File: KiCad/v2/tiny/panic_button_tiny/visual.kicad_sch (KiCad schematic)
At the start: 1 part, among them U4 TPS61022

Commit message: [UPDATE] some connections in the schematic
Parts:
- removed U4: TPS61022, Package_DFN_QFN:Texas_RWU0007A_VQFN-7_2x2mm_P0.5mm, symbol Converter_DCDC:TPS61022
- added D1: WS2812B, PCM_SparkFun-LED:WS2812_2020, symbol PCM_SparkFun-LED:WS2812B_2020
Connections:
- net 3.3V: now also D1.4 (VDD)
- net GND: now also D1.2 (VSS)
- new net LED_DIN: D1.3 (DIN)
- no-connect marks 0 -> 1
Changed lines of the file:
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@@
 	(generator_version "10.0")
 	(paper "A4")
-	(wire
-		(pts
-			(xy 62.23 30.48) (xy 60.96 30.48)
-		)
-		(stroke
-			(width 0)
-			(type default)
-		)
-	)
-	(hierarchical_label "modem_status"
+	(no_connect
+		(at 52.07 31.75)
+	)
+	(hierarchical_label "LED_DIN"
 		(shape input)
-		(at 55.88 22.86 90)
+		(at 36.83 31.75 180)
 		(effects
 			(font
 				(size 1.27 1.27)
 			)
-			(justify left)
-		)
-	)
-	(hierarchical_label "modem_rail_switch"
-		(shape input)
-		(at 40.64 30.48 180)
-		(effects
-			(font
-				(size 1.27 1.27)
-			)
 			(justify right)
 		)
@@
 	(symbol
 		(lib_id "PCM_SparkFun-PowerSymbol:3.3V")
-		(at 45.72 22.86 0)
+		(at 44.45 24.13 0)
 		(unit 1)
 		(body_style 1)
@@
 		(dnp no)
 		(fields_autoplaced yes)
-		(property "Reference" "#PWR048"
-			(at 45.72 26.67 0)
+		(property "Reference" "#PWR064"
+			(at 44.45 27.94 0)
 			(hide yes)
 			(show_name no)
@@
 		)
 		(property "Value" "3.3V"
-			(at 45.72 19.05 0)
+			(at 44.45 20.32 0)
 			(show_name no)
 			(do_not_autoplace yes)
@@
 		)
 		(property "Footprint" ""
-			(at 45.72 22.86 0)
+			(at 44.45 24.13 0)
 			(hide yes)
 			(show_name no)
@@
 		)
 		(property "Datasheet" ""
-			(at 45.72 22.86 0)
+			(at 44.45 24.13 0)
 			(hide yes)
 			(show_name no)
@@
 		)
 		(property "Description" "Power symbol creates a global label with name \"3.3V\""
-			(at 45.72 29.21 0)
+			(at 44.45 30.48 0)
 			(hide yes)
 			(show_name no)
@@
 		(instances
 			(project "panic_button_tiny"
-				(path "/c4eb92e9-b42f-4db0-b1d9-0ef70f7ca601/5fcd7ab2-c492-450d-9345-ebba8273bb1f"
-					(reference "#PWR048")
+				(path "/c4eb92e9-b42f-4db0-b1d9-0ef70f7ca601/a5c86ac0-c7fd-4e96-b586-e8495a668fc4"
+					(reference "#PWR064")
 					(unit 1)
 				)
@@
 	)
 	(symbol
-		(lib_id "PCM_SparkFun-PowerSymbol:5V")
-		(at 62.23 30.48 0)
+		(lib_id "PCM_SparkFun-PowerSymbol:GND")
+		(at 44.45 39.37 0)
 		(unit 1)
 		(body_style 1)
@@
 		(dnp no)
 		(fields_autoplaced yes)
-		(property "Reference" "#PWR050"
-			(at 62.23 34.29 0)
-			(hide yes)
-			(show_name no)
-			(do_not_autoplace no)
-			(effects
-				(font
-					(size 1.27 1.27)
-				)
-			)
-		)
-		(property "Value" "5V"
-			(at 62.23 26.67 0)
+		(property "Reference" "#PWR065"
+			(at 44.45 45.72 0)
+			(hide yes)
+			(show_name no)
+			(do_not_autoplace no)
+			(effects
+				(font
+					(size 1.27 1.27)
+				)
+			)
+		)
+		(property "Value" "GND"
+			(at 44.45 43.18 0)
 			(show_name no)
 			(do_not_autoplace yes)
@@
 		)
 		(property "Footprint" ""
-			(at 62.23 30.48 0)
+			(at 44.45 39.37 0)
 			(hide yes)
 			(show_name no)
@@
 		)
 		(property "Datasheet" ""
-			(at 62.23 30.48 0)
-			(hide yes)
-			(show_name no)
-			(do_not_autoplace no)
-			(effects
-				(font
-					(size 1.27 1.27)
-				)
-			)
-		)
-		(property "Description" "Power symbol creates a global label with name \"5V\""
-			(at 62.23 36.83 0)
+			(at 44.45 39.37 0)
+			(hide yes)
+			(show_name no)
+			(do_not_autoplace no)
+			(effects
+				(font
+					(size 1.27 1.27)
+				)
+			)
+		)
+		(property "Description" "Power symbol creates a global label with name \"GND\" , ground"
+			(at 44.45 48.26 0)
 			(hide yes)
 			(show_name no)
@@
 		(instances
 			(project "panic_button_tiny"
-				(path "/c4eb92e9-b42f-4db0-b1d9-0ef70f7ca601/5fcd7ab2-c492-450d-9345-ebba8273bb1f"
-					(reference "#PWR050")
+				(path "/c4eb92e9-b42f-4db0-b1d9-0ef70f7ca601/a5c86ac0-c7fd-4e96-b586-e8495a668fc4"
+					(reference "#PWR065")
 					(unit 1)
 				)
@@
 	)
 	(symbol
-		(lib_id "Converter_DCDC:TPS61022")
-		(at 50.8 30.48 0)
+		(lib_id "PCM_SparkFun-LED:WS2812B_2020")
+		(at 44.45 31.75 0)
 		(unit 1)
 		(body_style 1)
@@
 		(dnp no)
 		(fields_autoplaced yes)
-		(property "Reference" "U4"
-			(at 52.9433 38.1 0)
-			(show_name no)
-			(do_not_autoplace no)
-			(effects
-				(font
-					(size 1.27 1.27)
-				)
-				(justify left)
-			)
-		)
-		(property "Value" "TPS61022"
-			(at 52.9433 40.64 0)
-			(show_name no)
-			(do_not_autoplace no)
-			(effects
-				(font
-					(size 1.27 1.27)
-				)
-				(justify left)
-			)
-		)
-		(property "Footprint" "Package_DFN_QFN:Texas_RWU0007A_VQFN-7_2x2mm_P0.5mm"
-			(at 50.8 53.34 0)
-			(hide yes)
-			(show_name no)
-			(do_not_autoplace no)
-			(effects
-				(font
-					(size 1.27 1.27)
-				)
-			)
-		)
-		(property "Datasheet" "https://www.ti.com/lit/ds/symlink/tps61022.pdf"
-			(at 50.8 55.88 0)
-			(hide yes)
-			(show_name no)
-			(do_not_autoplace no)
-			(effects
-				(font
-					(size 1.27 1.27)
-				)
-			)
-		)
-		(property "Description" "8A Boost Converter, 0.5-5.5 V input, 2.2-5.5V output, Texas RWU0007A VQFN-7"
-			(at 50.8 30.48 0)
-			(hide yes)
-			(show_name no)
-			(do_not_autoplace no)
-			(effects
-				(font
-					(size 1.27 1.27)
-				)
-			)
+		(property "Reference" "D1"
+			(at 52.07 27.8698 0)
+			(show_name no)
+			(do_not_autoplace no)
+			(effects
+				(font
+					(size 1.27 1.27)
+				)
+			)
+		)
+		(property "Value" "WS2812B"
+			(at 49.53 38.1 0)
+			(show_name no)
+			(do_not_autoplace yes)
+			(effects
+				(font
+					(size 1.27 1.27)
+				)
+			)
+		)
+		(property "Footprint" "PCM_SparkFun-LED:WS2812_2020"
+			(at 44.45 41.91 0)
+			(hide yes)
+			(show_name no)
+			(do_not_autoplace no)
+			(effects
+				(font
+					(size 1.27 1.27)
+				)
+			)
+		)
+		(property "Datasheet" "https://cdn.sparkfun.com/assets/e/1/0/f/b/WS2812C-2020_V1.2_EN_19112716191654.pdf"
+			(at 44.45 46.99 0)
+			(hide yes)
+			(show_name no)
+			(do_not_autoplace no)
+			(effects
+				(font
+					(size 1.27 1.27)
+				)
+			)
+		)
+		(property "Description" "RGB LED with integrated controller"
+			(at 44.45 49.53 0)
+			(hide yes)
+			(show_name no)
+			(do_not_autoplace no)
+			(effects
+				(font
+					(size 1.27 1.27)
+				)
+			)
+		)
+		(property "PROD_ID" "DIO-15591"
+			(at 44.45 44.45 0)
+			(hide yes)
+			(show_name no)
+			(do_not_autoplace no)
+			(effects
+				(font
+					(size 1.27 1.27)
+				)
+			)
+		)
+		(pin "4"
+		)
+		(pin "3"
 		)
 		(pin "2"
 		)
-		(pin "4"
-		)
-		(pin "7"
-		)
-		(pin "6"
-		)
 		(pin "1"
-		)
-		(pin "3"
-		)
-		(pin "5"
 		)
 		(instances
 			(project "panic_button_tiny"
-				(path "/c4eb92e9-b42f-4db0-b1d9-0ef70f7ca601/5fcd7ab2-c492-450d-9345-ebba8273bb1f"
-					(reference "U4")
+				(path "/c4eb92e9-b42f-4db0-b1d9-0ef70f7ca601/a5c86ac0-c7fd-4e96-b586-e8495a668fc4"
+					(reference "D1")
 					(unit 1)
 				)
-			)
-		)
-	)
-	(symbol
-		(lib_id "PCM_SparkFun-PowerSymbol:GND")
-		(at 50.8 38.1 0)
-		(unit 1)
-		(body_style 1)
-		(exclude_from_sim no)
-		(in_bom yes)
-		(on_board yes)
-		(in_pos_files yes)
-		(dnp no)
-		(fields_autoplaced yes)
-		(property "Reference" "#PWR049"
-			(at 50.8 44.45 0)
-			(hide yes)
-			(show_name no)
-			(do_not_autoplace no)
-			(effects
-				(font
-					(size 1.27 1.27)
-				)
-			)
-		)
-		(property "Value" "GND"
-			(at 50.8 41.91 0)
-			(show_name no)
-			(do_not_autoplace yes)
-			(effects
-				(font
-					(size 1.27 1.27)
-				)
-			)
-		)
-		(property "Footprint" ""
-			(at 50.8 38.1 0)
-			(hide yes)
-			(show_name no)
-			(do_not_autoplace no)
-			(effects
-				(font
-					(size 1.27 1.27)
-				)
-			)
-		)
-		(property "Datasheet" ""
-			(at 50.8 38.1 0)
-			(hide yes)
-			(show_name no)
-			(do_not_autoplace no)
-			(effects
-				(font
-					(size 1.27 1.27)
-				)
-			)
-		)
-		(property "Description" "Power symbol creates a global label with name \"GND\" , ground"
-			(at 50.8 46.99 0)
-			(hide yes)
-			(show_name no)
-			(do_not_autoplace no)
-			(effects
-				(font
-					(size 1.27 1.27)
-				)
-			)
-		)
-		(pin "1"
-		)
-		(instances
-			(project "panic_button_tiny"
-				(path "/c4eb92e9-b42f-4db0-b1d9-0ef70f7ca601/5fcd7ab2-c492-450d-9345-ebba8273bb1f"
-					(reference "#PWR049")
-					(unit 1)
-				)

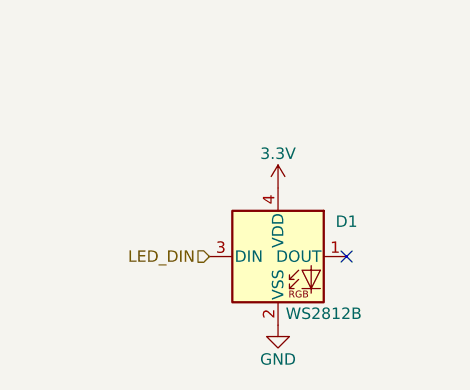
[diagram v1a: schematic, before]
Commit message: [UPDATE] connections in the circuit schematic
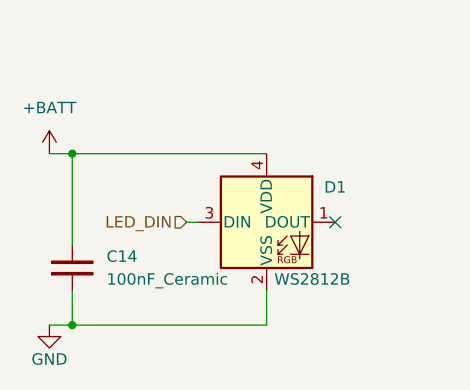
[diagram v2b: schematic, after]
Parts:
- added C14: 100nF_Ceramic, Capacitor_THT:C_Disc_D5.0mm_W2.5mm_P2.50mm, symbol PCM_SL_Capacitors:100nF_Ceramic
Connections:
- net GND: now also C14.1
- net 3.3V renamed +BATT
- net +BATT: now also C14.2
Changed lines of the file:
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@@
 	(generator_version "10.0")
 	(paper "A4")
+	(junction
+		(at 21.59 20.32)
+		(diameter 0)
+		(color 0 0 0 0)
+	)
+	(junction
+		(at 21.59 39.37)
+		(diameter 0)
+		(color 0 0 0 0)
+	)
 	(no_connect
-		(at 52.07 31.75)
+		(at 50.8 27.94)
+	)
+	(wire
+		(pts
+			(xy 43.18 39.37) (xy 43.18 35.56)
+		)
+		(stroke
+			(width 0)
+			(type default)
+		)
+	)
+	(wire
+		(pts
+			(xy 21.59 39.37) (xy 43.18 39.37)
+		)
+		(stroke
+			(width 0)
+			(type default)
+		)
+	)
+	(wire
+		(pts
+			(xy 21.59 30.48) (xy 21.59 20.32)
+		)
+		(stroke
+			(width 0)
+			(type default)
+		)
+	)
+	(wire
+		(pts
+			(xy 19.05 39.37) (xy 21.59 39.37)
+		)
+		(stroke
+			(width 0)
+			(type default)
+		)
+	)
+	(wire
+		(pts
+			(xy 21.59 35.56) (xy 21.59 39.37)
+		)
+		(stroke
+			(width 0)
+			(type default)
+		)
+	)
+	(wire
+		(pts
+			(xy 34.29 27.94) (xy 35.56 27.94)
+		)
+		(stroke
+			(width 0)
+			(type default)
+		)
+	)
+	(wire
+		(pts
+			(xy 19.05 20.32) (xy 21.59 20.32)
+		)
+		(stroke
+			(width 0)
+			(type default)
+		)
+	)
+	(wire
+		(pts
+			(xy 21.59 20.32) (xy 43.18 20.32)
+		)
+		(stroke
+			(width 0)
+			(type default)
+		)
 	)
 	(hierarchical_label "LED_DIN"
 		(shape input)
-		(at 36.83 31.75 180)
+		(at 34.29 27.94 180)
 		(effects
 			(font
@@
 	)
 	(symbol
-		(lib_id "PCM_SparkFun-PowerSymbol:3.3V")
-		(at 44.45 24.13 0)
+		(lib_id "PCM_SparkFun-PowerSymbol:GND")
+		(at 19.05 39.37 0)
 		(unit 1)
 		(body_style 1)
@@
 		(dnp no)
 		(fields_autoplaced yes)
-		(property "Reference" "#PWR064"
-			(at 44.45 27.94 0)
-			(hide yes)
-			(show_name no)
-			(do_not_autoplace no)
-			(effects
-				(font
-					(size 1.27 1.27)
-				)
-			)
-		)
-		(property "Value" "3.3V"
-			(at 44.45 20.32 0)
+		(property "Reference" "#PWR066"
+			(at 19.05 45.72 0)
+			(hide yes)
+			(show_name no)
+			(do_not_autoplace no)
+			(effects
+				(font
+					(size 1.27 1.27)
+				)
+			)
+		)
+		(property "Value" "GND"
+			(at 19.05 43.18 0)
 			(show_name no)
 			(do_not_autoplace yes)
@@
 		)
 		(property "Footprint" ""
-			(at 44.45 24.13 0)
+			(at 19.05 39.37 0)
 			(hide yes)
 			(show_name no)
@@
 		)
 		(property "Datasheet" ""
-			(at 44.45 24.13 0)
-			(hide yes)
-			(show_name no)
-			(do_not_autoplace no)
-			(effects
-				(font
-					(size 1.27 1.27)
-				)
-			)
-		)
-		(property "Description" "Power symbol creates a global label with name \"3.3V\""
-			(at 44.45 30.48 0)
+			(at 19.05 39.37 0)
+			(hide yes)
+			(show_name no)
+			(do_not_autoplace no)
+			(effects
+				(font
+					(size 1.27 1.27)
+				)
+			)
+		)
+		(property "Description" "Power symbol creates a global label with name \"GND\" , ground"
+			(at 19.05 48.26 0)
 			(hide yes)
 			(show_name no)
@@
 			(project "panic_button_tiny"
 				(path "/c4eb92e9-b42f-4db0-b1d9-0ef70f7ca601/a5c86ac0-c7fd-4e96-b586-e8495a668fc4"
-					(reference "#PWR064")
+					(reference "#PWR066")
 					(unit 1)
 				)
@@
 	)
 	(symbol
-		(lib_id "PCM_SparkFun-PowerSymbol:GND")
-		(at 44.45 39.37 0)
+		(lib_id "power:+BATT")
+		(at 19.05 20.32 0)
 		(unit 1)
 		(body_style 1)
@@
 		(fields_autoplaced yes)
 		(property "Reference" "#PWR065"
-			(at 44.45 45.72 0)
-			(hide yes)
-			(show_name no)
-			(do_not_autoplace no)
-			(effects
-				(font
-					(size 1.27 1.27)
-				)
-			)
-		)
-		(property "Value" "GND"
-			(at 44.45 43.18 0)
-			(show_name no)
-			(do_not_autoplace yes)
+			(at 19.05 24.13 0)
+			(hide yes)
+			(show_name no)
+			(do_not_autoplace no)
+			(effects
+				(font
+					(size 1.27 1.27)
+				)
+			)
+		)
+		(property "Value" "+BATT"
+			(at 19.05 15.24 0)
+			(show_name no)
+			(do_not_autoplace no)
 			(effects
 				(font
@@
 		)
 		(property "Footprint" ""
-			(at 44.45 39.37 0)
+			(at 19.05 20.32 0)
 			(hide yes)
 			(show_name no)
@@
 		)
 		(property "Datasheet" ""
-			(at 44.45 39.37 0)
-			(hide yes)
-			(show_name no)
-			(do_not_autoplace no)
-			(effects
-				(font
-					(size 1.27 1.27)
-				)
-			)
-		)
-		(property "Description" "Power symbol creates a global label with name \"GND\" , ground"
-			(at 44.45 48.26 0)
+			(at 19.05 20.32 0)
+			(hide yes)
+			(show_name no)
+			(do_not_autoplace no)
+			(effects
+				(font
+					(size 1.27 1.27)
+				)
+			)
+		)
+		(property "Description" "Power symbol creates a global label with name \"+BATT\""
+			(at 19.05 20.32 0)
 			(hide yes)
 			(show_name no)
@@
 	(symbol
 		(lib_id "PCM_SparkFun-LED:WS2812B_2020")
-		(at 44.45 31.75 0)
+		(at 43.18 27.94 0)
 		(unit 1)
 		(body_style 1)
@@
 		(fields_autoplaced yes)
 		(property "Reference" "D1"
-			(at 52.07 27.8698 0)
+			(at 50.8 24.0598 0)
 			(show_name no)
 			(do_not_autoplace no)
@@
 		)
 		(property "Value" "WS2812B"
-			(at 49.53 38.1 0)
+			(at 48.26 34.29 0)
 			(show_name no)
 			(do_not_autoplace yes)
@@
 		)
 		(property "Footprint" "PCM_SparkFun-LED:WS2812_2020"
-			(at 44.45 41.91 0)
+			(at 43.18 38.1 0)
 			(hide yes)
 			(show_name no)
@@
 		)
 		(property "Datasheet" "https://cdn.sparkfun.com/assets/e/1/0/f/b/WS2812C-2020_V1.2_EN_19112716191654.pdf"
-			(at 44.45 46.99 0)
+			(at 43.18 43.18 0)
 			(hide yes)
 			(show_name no)
@@
 		)
 		(property "Description" "RGB LED with integrated controller"
-			(at 44.45 49.53 0)
+			(at 43.18 45.72 0)
 			(hide yes)
 			(show_name no)
@@
 		)
 		(property "PROD_ID" "DIO-15591"
-			(at 44.45 44.45 0)
+			(at 43.18 40.64 0)
 			(hide yes)
 			(show_name no)
@@
 					(unit 1)
 				)
+			)
+		)
+	)
+	(symbol
+		(lib_id "PCM_SL_Capacitors:100nF_Ceramic")
+		(at 21.59 33.02 90)
+		(unit 1)
+		(body_style 1)
+		(exclude_from_sim no)
+		(in_bom yes)
+		(on_board yes)
+		(in_pos_files yes)
+		(dnp no)
+		(fields_autoplaced yes)
+		(property "Reference" "C14"
+			(at 25.4 31.7499 90)
+			(show_name no)
+			(do_not_autoplace no)
+			(effects
+				(font
+					(size 1.27 1.27)
+				)
+				(justify right)
+			)
+		)
+		(property "Value" "100nF_Ceramic"
+			(at 25.4 34.2899 90)
+			(show_name no)
+			(do_not_autoplace no)
+			(effects
+				(font
+					(size 1.27 1.27)
+				)
+				(justify right)
+			)
+		)
+		(property "Footprint" "Capacitor_THT:C_Disc_D5.0mm_W2.5mm_P2.50mm"
+			(at 25.4 33.02 0)
+			(hide yes)
+			(show_name no)
+			(do_not_autoplace no)
+			(effects
+				(font
+					(size 1.27 1.27)
+				)
+			)
+		)
+		(property "Datasheet" ""
+			(at 21.59 33.02 0)
+			(hide yes)
+			(show_name no)
+			(do_not_autoplace no)
+			(effects
+				(font
+					(size 1.27 1.27)
+				)
+			)
+		)
+		(property "Description" "100nF Ceramic Capacitor"
+			(at 21.59 33.02 0)
+			(hide yes)
+			(show_name no)
+			(do_not_autoplace no)
+			(effects
+				(font
+					(size 1.27 1.27)
+				)
+			)
+		)
+		(pin "2"
+		)
+		(pin "1"
+		)
+		(instances
+			(project "panic_button_tiny"
+				(path "/c4eb92e9-b42f-4db0-b1d9-0ef70f7ca601/a5c86ac0-c7fd-4e96-b586-e8495a668fc4"
+					(reference "C14")
+					(unit 1)
+				)

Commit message: [UPDATE] the schematics annotations
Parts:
- renumbered C14 to C10
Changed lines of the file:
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@@
 		(dnp no)
 		(fields_autoplaced yes)
-		(property "Reference" "C14"
+		(property "Reference" "C10"
 			(at 25.4 31.7499 90)
 			(show_name no)
@@
 			(project "panic_button_tiny"
 				(path "/c4eb92e9-b42f-4db0-b1d9-0ef70f7ca601/a5c86ac0-c7fd-4e96-b586-e8495a668fc4"
-					(reference "C14")
+					(reference "C10")
 					(unit 1)
 				)

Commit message: [UPDATE] connections in the schematic to better represent the logic flow
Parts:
- renumbered C10 to C12
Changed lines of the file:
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@@
 		(dnp no)
 		(fields_autoplaced yes)
-		(property "Reference" "#PWR069"
+		(property "Reference" "#PWR072"
 			(at 19.05 45.72 0)
 			(hide yes)
@@
 			(project "panic_button_tiny"
 				(path "/c4eb92e9-b42f-4db0-b1d9-0ef70f7ca601/a5c86ac0-c7fd-4e96-b586-e8495a668fc4"
-					(reference "#PWR069")
+					(reference "#PWR072")
 					(unit 1)
 				)
@@
 		(dnp no)
 		(fields_autoplaced yes)
-		(property "Reference" "#PWR068"
+		(property "Reference" "#PWR071"
 			(at 19.05 24.13 0)
 			(hide yes)
@@
 			(project "panic_button_tiny"
 				(path "/c4eb92e9-b42f-4db0-b1d9-0ef70f7ca601/a5c86ac0-c7fd-4e96-b586-e8495a668fc4"
-					(reference "#PWR068")
+					(reference "#PWR071")
 					(unit 1)
 				)
@@
 		(dnp no)
 		(fields_autoplaced yes)
-		(property "Reference" "C10"
+		(property "Reference" "C12"
 			(at 25.4 31.7499 90)
 			(show_name no)
@@
 			(project "panic_button_tiny"
 				(path "/c4eb92e9-b42f-4db0-b1d9-0ef70f7ca601/a5c86ac0-c7fd-4e96-b586-e8495a668fc4"
-					(reference "C10")
+					(reference "C12")
 					(unit 1)
 				)
